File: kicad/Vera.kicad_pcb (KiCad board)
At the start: 4 copper layers, 69.8 x 58 mm, 41 parts, among them Q1 AO3400, T1 Wurth 749010012A, T2 Wurth 749010012A, U1 TI AM62A7, U2 Microchip KSZ9477, U3 TI MSPM0G3507, U4 TI ISOW1044BDFMR, U5 Infineon SLB9670, Y1 25MHz

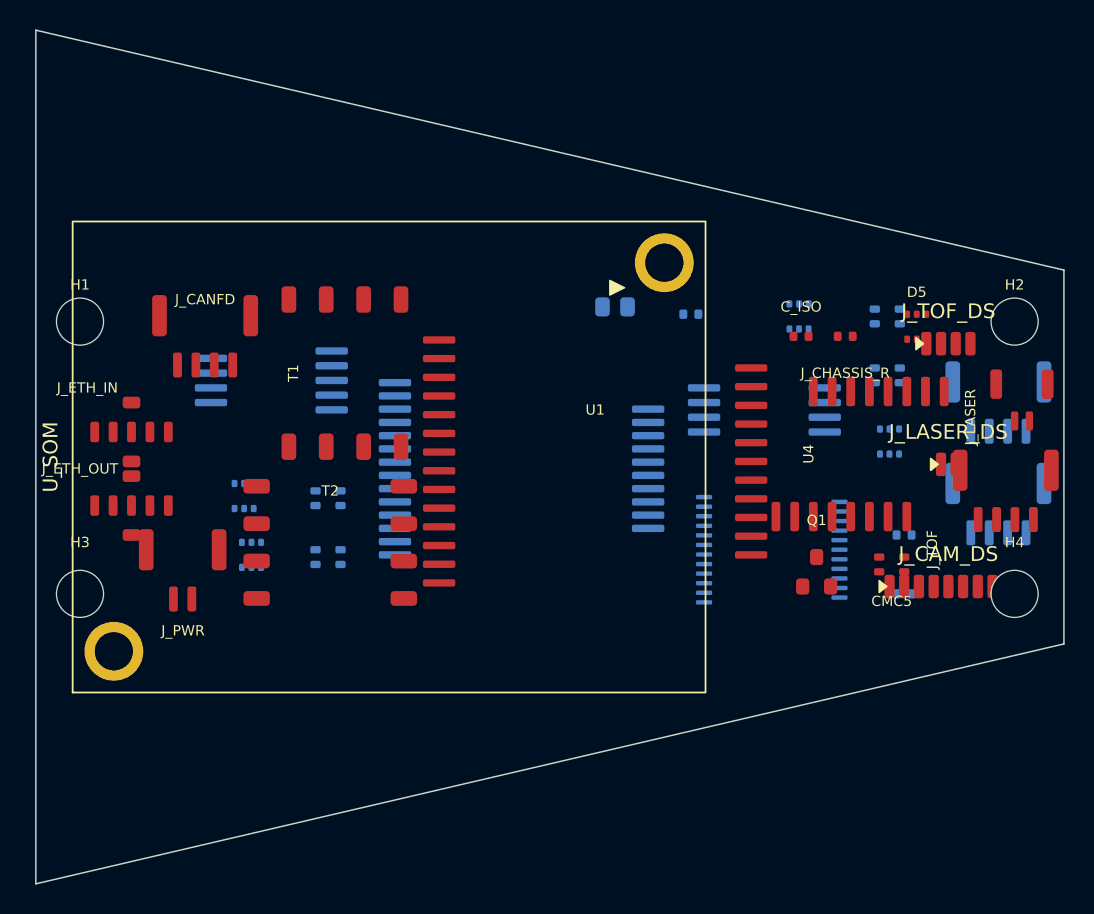
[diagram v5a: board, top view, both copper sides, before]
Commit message: Vera PCB: corner mounting holes + concentric rounded corners + install keep-outs
Per user: moved mounting holes to the 4 trapezoid corners and rounded each corner
with an arc CONCENTRIC to its M2.5 hole; added ~1/16in (1.5875mm) component-clear
keep-out strips along the port and starboard edges for the nose install rails.

mod_vera_corners.py: fillets each corner (R=3mm), places an M2.5 NPTH (Ø2.7) at each
fillet centre (arc concentric with the hole), and adds a keep-out rule area
(no footprints / no copper pour) + F.SilkS boundary along the port (C1-C2) and
starboard (C3-C0) slanted edges. Board loads (pre-commit guard); invalid_outline=0.
Corner holes at (66.8,2.4)/(66.8,23.0)/(3.0,37.9)/(3.0,-12.5).

Co-Authored-By: Claude Opus 4.8 <noreply@anthropic.com>
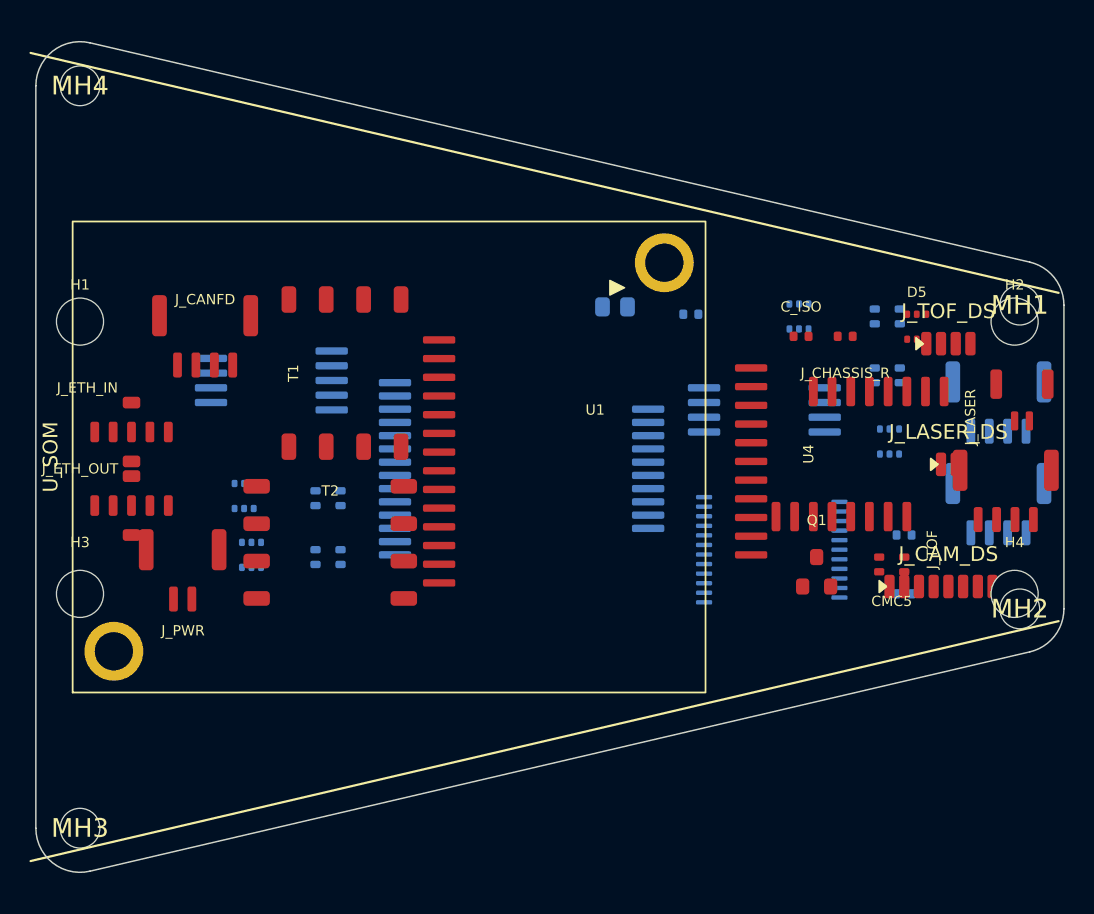
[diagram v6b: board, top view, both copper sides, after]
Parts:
- added MH1: , , F.Cu at (66.8, 2.38)
- added MH2: , , F.Cu at (66.8, 23.0)
- added MH3: , , F.Cu at (3.00, 37.9)
- added MH4: , , F.Cu at (3.00, -12.5)
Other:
- board size 69.8 x 58 mm -> 69.8 x 56.4 mm
